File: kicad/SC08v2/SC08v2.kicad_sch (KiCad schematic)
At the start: 25 parts

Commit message: Improve and fix docs
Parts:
- ADR0_U0, ADR0_U1, IC_U1, RAM_U1: value ~ -> (none)

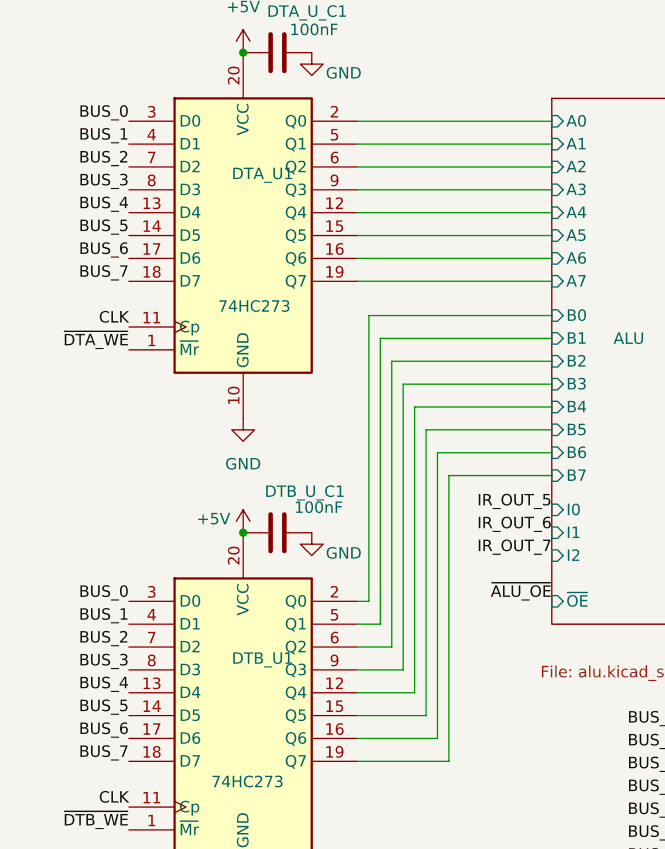
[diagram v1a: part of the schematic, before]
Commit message: Improve docs and schemas
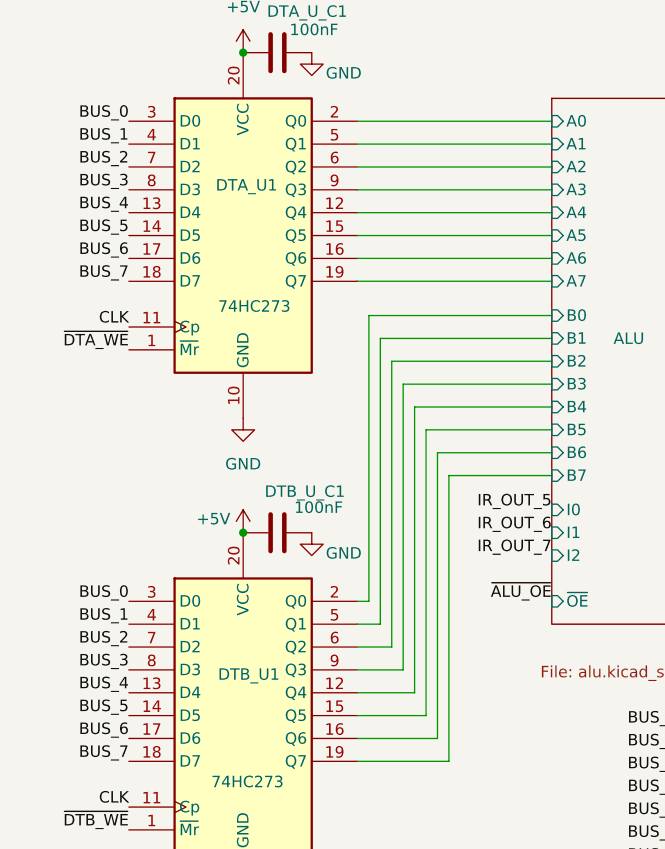
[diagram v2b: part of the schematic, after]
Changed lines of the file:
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@@
 		(dnp no)
 		(property "Reference" "DTA_U1"
-			(at 36.83 35.052 0)
+			(at 35.052 36.322 0)
 			(show_name no)
 			(do_not_autoplace no)
@@
 		(dnp no)
 		(property "Reference" "DTB_U1"
-			(at 36.83 88.9 0)
+			(at 35.306 90.678 0)
 			(show_name no)
 			(do_not_autoplace no)
